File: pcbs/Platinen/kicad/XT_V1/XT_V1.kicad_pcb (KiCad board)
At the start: 4 copper layers, 100 x 77 mm, 79 parts, among them J1 Conn_01x04, J10 TBL009-500-02GY-2GY, J2 Conn_01x02, J3 Conn_01x02, J4 Conn_02x03_Odd_Even, J5 Conn_02x05_Odd_Even, J6 Conn_02x05_Odd_Even, J7 TBL009-500-02GY-2GY, J8 TBL009-500-02GY-2GY, J9 TBL009-500-02GY-2GY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

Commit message: Redesign XT V1
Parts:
- added D1: SM4007, Diode_SMD:D_MELF, F.Cu at (131.8, 86.6)
- added D2: SM4007, Diode_SMD:D_MELF, F.Cu at (137.4, 86.6)
- added Q10: BT136-500, Package_TO_SOT_THT:TO-220-3_Vertical, F.Cu at (154.7, 77.2)
- added Q9: BT136-500, Package_TO_SOT_THT:TO-220-3_Vertical, F.Cu at (144.8, 77.2)
- added R32: 330, Resistor_SMD:R_0805_2012Metric_Pad1.20x1.40mm_HandSolder, F.Cu at (156.7, 87.4)
- added R33: 56k, Resistor_SMD:R_MELF_MMB-0207, F.Cu at (131.8, 79.2)
- added R34: 56k, Resistor_SMD:R_MELF_MMB-0207, F.Cu at (137.4, 79.2)
- added R35: 68, Resistor_SMD:R_0805_2012Metric_Pad1.20x1.40mm_HandSolder, F.Cu at (121.9, 75.7)
- added R36: 68, Resistor_SMD:R_0805_2012Metric_Pad1.20x1.40mm_HandSolder, F.Cu at (142.2, 75.7)
- added R37: 68, Resistor_SMD:R_0805_2012Metric_Pad1.20x1.40mm_HandSolder, F.Cu at (152.1, 75.7)
- added U10: MOC3043M, Package_DIP:DIP-6_W8.89mm_SMDSocket_LongPads, F.Cu at (154.2, 96.3)
- added U9: MOC3043M, Package_DIP:DIP-6_W8.89mm_SMDSocket_LongPads, F.Cu at (144.3, 96.3)
- Q5, Q7: value BT136-500 -> BC846; footprint Package_TO_SOT_THT:TO-220-3_Vertical -> Package_TO_SOT_SMD:SOT-23
- R17, R18: value max 360 -> 1k
- R20, R22: value 360 -> max 360
- R23: value 360 -> 1k
- R24: value 330 -> 1k
- R26, R27: value 330 -> 360
- R28: value 68 -> 360
- R30, R31: value 68 -> 330
- U6, U8: value MOC3043M -> TLP291; footprint Package_DIP:DIP-6_W8.89mm_SMDSocket_LongPads -> Package_SO:SOIC-4_4.55x2.6mm_P1.27mm
- moved R28 38.4 mm to (151.6, 87.4), turned to 270 degrees
- moved Q5 37.7 mm to (144.3, 104.6), turned to 90 degrees
- moved R20 31.3 mm to (141.5, 104.9)
- moved Q7 30.1 mm to (154.2, 104.6), turned to 90 degrees
- moved R19 26.4 mm to (122.9, 104.9)
- moved Q4 26.4 mm to (125.7, 104.9)
- moved R15 26.4 mm to (125.7, 107.7)
- moved Q8 25.4 mm to (126.7, 77.2)
- moved R24 22.8 mm to (138.2, 101.9), turned to 0 degrees
- moved R23 22.8 mm to (131.8, 101.9), turned to 0 degrees
- moved R22 21.7 mm to (151.4, 104.9)
- moved R26 20.1 mm to (123.2, 87.4)
- moved R17 18.0 mm to (144.3, 107.4), turned to 0 degrees
- moved C16 17.6 mm to (113.8, 72.4)
- moved R30 17.2 mm to (128.3, 87.4), turned to 270 degrees
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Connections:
- J10 pad 1: Net-(J10-Pad1) -> Net-(C17-Pad2)
- J10 pad 2: Net-(J10-Pad1) -> Net-(C17-Pad2)
- J7 pad 1: Net-(J7-Pad1) -> Net-(D1-Pad2)
- J7 pad 2: Net-(J7-Pad1) -> Net-(D1-Pad2)
- J7 pad 3: Net-(C15-Pad2) -> Net-(J7-Pad3)
- J7 pad 4: Net-(C15-Pad2) -> Net-(J7-Pad3)
- J8 pad 1: Net-(J8-Pad1) -> Net-(C16-Pad2)
- J8 pad 2: Net-(J8-Pad1) -> Net-(C16-Pad2)
- J8 pad 3: Net-(C16-Pad2) -> Net-(C15-Pad2)
- J8 pad 4: Net-(C16-Pad2) -> Net-(C15-Pad2)
- J9 pad 1: Net-(J9-Pad1) -> Net-(D2-Pad2)
- J9 pad 2: Net-(J9-Pad1) -> Net-(D2-Pad2)
- J9 pad 3: Net-(C17-Pad2) -> Net-(J9-Pad3)
- J9 pad 4: Net-(C17-Pad2) -> Net-(J9-Pad3)
- Q2 pad 3: Net-(Q2-Pad3) -> ZC1
- Q3 pad 3: Net-(Q3-Pad3) -> ZC2
- Q5 pad 1: Net-(C15-Pad2) -> Net-(Q5-Pad1)
- Q5 pad 2: Net-(J7-Pad1) -> GND
- Q6 pad 2: Net-(J8-Pad1) -> Net-(D1-Pad2)
- Q7 pad 1: Net-(C17-Pad2) -> Net-(Q7-Pad1)
- Q7 pad 2: Net-(J9-Pad1) -> GND
- Q8 pad 1: Net-(C18-Pad2) -> Net-(C15-Pad2)
- Q8 pad 2: Net-(J10-Pad1) -> Net-(D1-Pad2)
- R13 pad 1: Net-(Q2-Pad1) -> +3V3
- R13 pad 2: CH2 -> ZC1
- R14 pad 1: Net-(Q3-Pad1) -> +3V3
- R14 pad 2: CH3 -> ZC2
- R15 pad 2: CH4 -> CH2
- R17 pad 1: Net-(R17-Pad1) -> Net-(Q5-Pad1)
- R17 pad 2: VCC -> CH3
- R18 pad 1: Net-(R18-Pad1) -> Net-(Q7-Pad1)
- R18 pad 2: VCC -> CH4
- R20 pad 1: Net-(J7-Pad1) -> Net-(R20-Pad1)
- R20 pad 2: Net-(R20-Pad2) -> VCC
- R21 pad 1: Net-(J8-Pad1) -> Net-(D1-Pad2)
- R22 pad 1: Net-(J9-Pad1) -> Net-(R22-Pad1)
- R22 pad 2: Net-(R22-Pad2) -> VCC
- R23 pad 1: Net-(J10-Pad1) -> Net-(R23-Pad1)
- R23 pad 2: Net-(R23-Pad2) -> Net-(Q2-Pad1)
- R24 pad 1: Net-(C15-Pad2) -> Net-(R24-Pad1)
- R24 pad 2: Net-(Q5-Pad3) -> Net-(Q3-Pad1)
- R26 pad 1: Net-(C17-Pad2) -> Net-(D1-Pad2)
- R26 pad 2: Net-(Q7-Pad3) -> Net-(R26-Pad2)
- R27 pad 1: Net-(C18-Pad2) -> Net-(D2-Pad2)
- R27 pad 2: Net-(Q8-Pad3) -> Net-(R27-Pad2)
- R28 pad 1: Net-(J7-Pad1) -> Net-(D2-Pad2)
- R28 pad 2: Net-(C15-Pad1) -> Net-(R28-Pad2)
- R29 pad 1: Net-(J8-Pad1) -> Net-(D1-Pad2)
- R30 pad 1: Net-(J9-Pad1) -> Net-(C15-Pad2)
- R30 pad 2: Net-(C17-Pad1) -> Net-(Q8-Pad3)
- R31 pad 1: Net-(J10-Pad1) -> Net-(C17-Pad2)
- R31 pad 2: Net-(C18-Pad1) -> Net-(Q9-Pad3)
- U3 pad 33: Net-(U3-Pad33) -> ZC1
- U3 pad 38: Net-(U3-Pad38) -> ZC2
- U5 pad 4: Net-(Q5-Pad3) -> Net-(Q6-Pad3)
- U5 pad 6: Net-(R20-Pad2) -> Net-(R21-Pad2)
- U6 pad 1: Net-(R17-Pad1) -> Net-(D1-Pad1)
- U6 pad 2: Net-(Q2-Pad3) -> Net-(D1-Pad2)
- U6 pad 3: Net-(U6-Pad3) -> Net-(R23-Pad1)
- U6 pad 4: Net-(Q6-Pad3) -> VCC
- U7 pad 1: Net-(R18-Pad1) -> Net-(R19-Pad1)
- U7 pad 2: Net-(Q3-Pad3) -> Net-(Q4-Pad3)
- U7 pad 4: Net-(Q7-Pad3) -> Net-(Q8-Pad3)
- U7 pad 6: Net-(R22-Pad2) -> Net-(R26-Pad2)
- U8 pad 1: Net-(R19-Pad1) -> Net-(D2-Pad1)
- U8 pad 2: Net-(Q4-Pad3) -> Net-(D2-Pad2)
- U8 pad 3: Net-(U8-Pad3) -> Net-(R24-Pad1)
- U8 pad 4: Net-(Q8-Pad3) -> VCC
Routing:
- net Net-(D1-Pad2): track 0.00 -> 74.9 mm, vias 0 -> 2
- net Net-(D2-Pad2): track 0.00 -> 72.1 mm, vias 0 -> 2
- net ZC1: track 0.00 -> 35.6 mm, vias 0 -> 2
- net ZC2: track 0.00 -> 26.8 mm, vias 0 -> 2
- net Net-(J10-Pad1): track 26.8 -> 0.00 mm
- net Net-(J8-Pad1): track 26.7 -> 0.00 mm
- net Net-(J7-Pad1): track 26.6 -> 0.00 mm
- net Net-(J9-Pad1): track 26.6 -> 0.00 mm
- net Net-(J9-Pad3): track 0.00 -> 15.5 mm
- net Net-(D1-Pad1): track 0.00 -> 13.8 mm
- net VCC: track 133.4 -> 147.1 mm, vias 5 -> 6
- net Net-(D2-Pad1): track 0.00 -> 13.4 mm
- net Net-(J7-Pad3): track 0.00 -> 13.2 mm
- net Net-(Q9-Pad3): track 0.00 -> 11.1 mm
- net Net-(Q10-Pad3): track 0.00 -> 11.1 mm
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
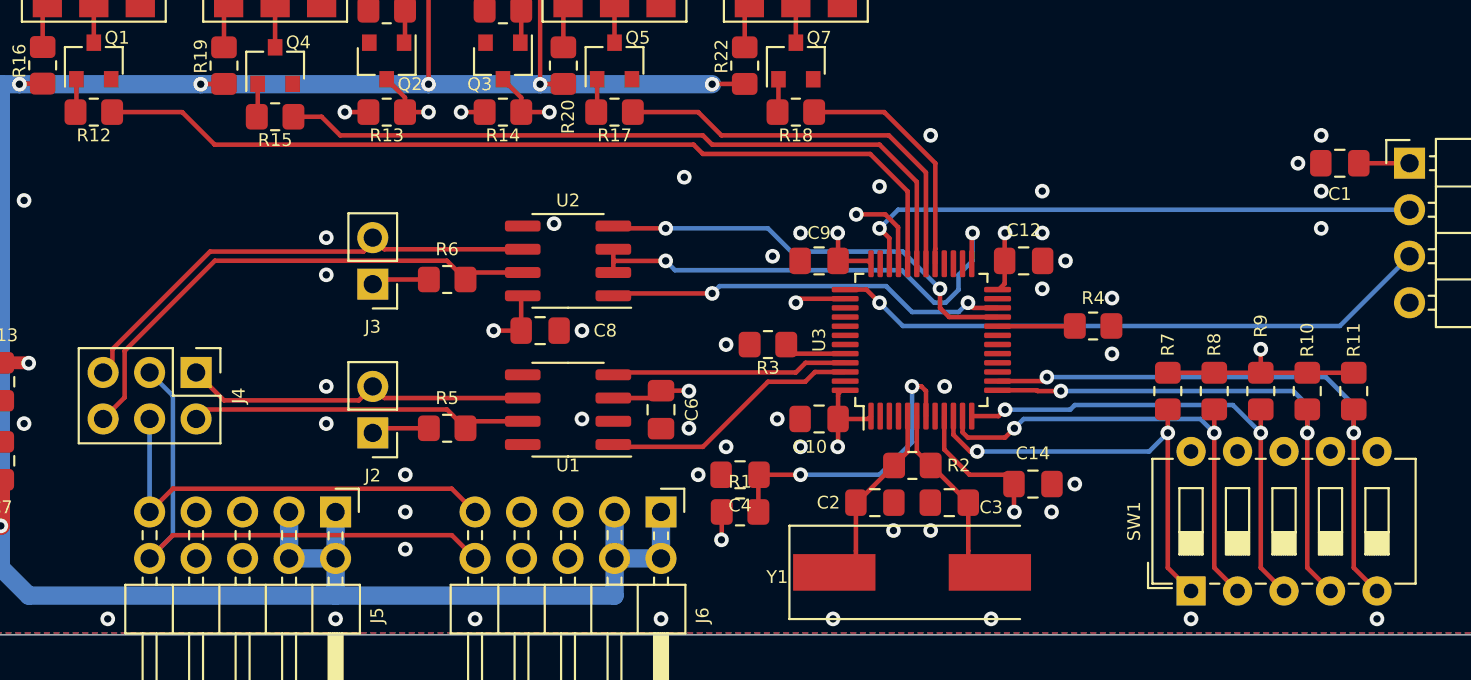
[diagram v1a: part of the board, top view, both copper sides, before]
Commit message: fix error in Schematic
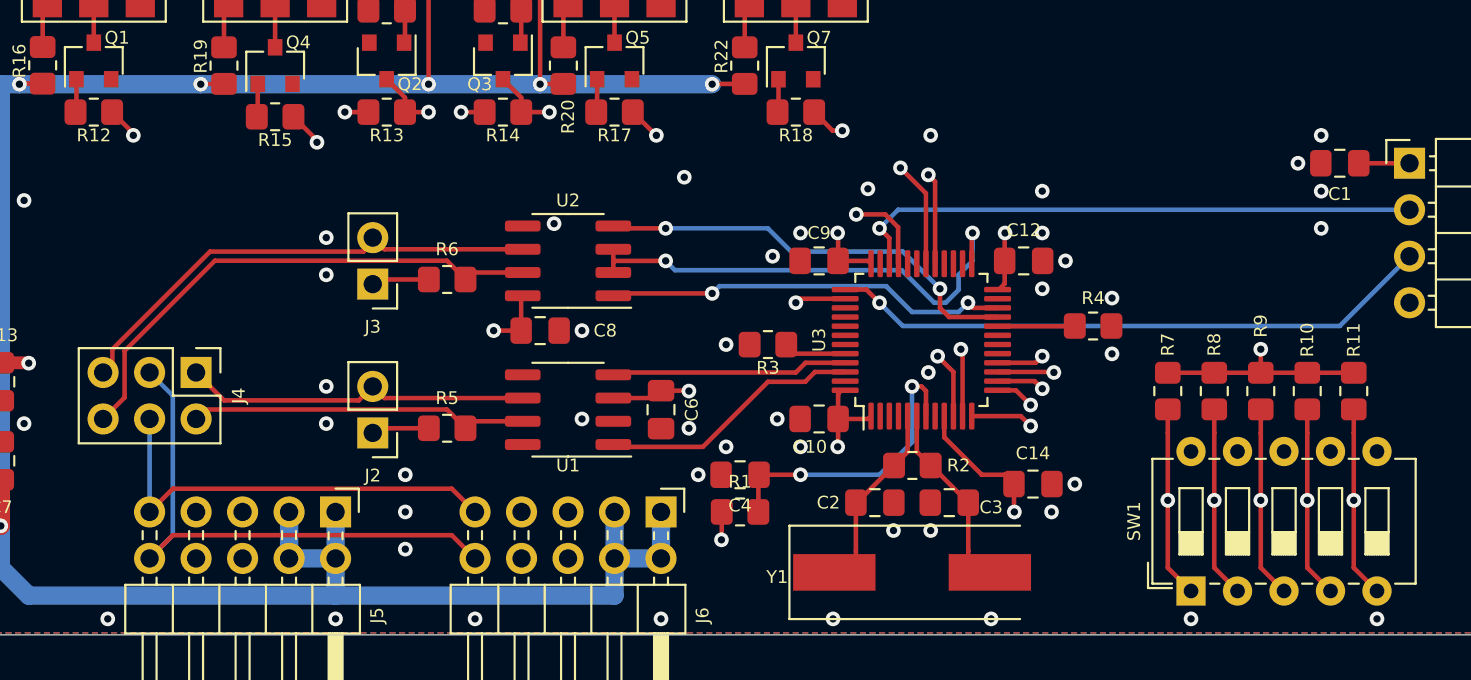
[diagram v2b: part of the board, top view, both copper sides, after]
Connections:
- U3 pad 10: Net-(R7-Pad1) -> CH3
- U3 pad 11: Net-(R8-Pad1) -> CH4
- U3 pad 12: Net-(R9-Pad1) -> Net-(R7-Pad1)
- U3 pad 13: Net-(R10-Pad1) -> Net-(R8-Pad1)
- U3 pad 14: Net-(R11-Pad1) -> Net-(R9-Pad1)
- U3 pad 15: Net-(U3-Pad15) -> Net-(R10-Pad1)
- U3 pad 16: Net-(U3-Pad16) -> Net-(R11-Pad1)
- U3 pad 29: CH4 -> CH1
- U3 pad 30: CH3 -> CH2
- U3 pad 31: CH2 -> Net-(U3-Pad31)
- U3 pad 32: CH1 -> Net-(U3-Pad32)
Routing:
- net CH4: track 13.3 -> 20.3 mm, vias 0 -> 2
- net CH3: track 22.4 -> 27.5 mm, vias 0 -> 2
- net Net-(R11-Pad1): track 31.9 -> 35.1 mm
- net Net-(R10-Pad1): track 29.0 -> 32.1 mm
- net Net-(R9-Pad1): track 26.9 -> 29.4 mm
- net CH1: track 49.2 -> 51.4 mm, vias 0 -> 2
- net Net-(R8-Pad1): track 25.7 -> 26.6 mm
- net Net-(R7-Pad1): track 23.7 -> 22.8 mm
- net CH2: track 40.0 -> 40.2 mm, vias 0 -> 2

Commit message: started revs
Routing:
- net DIR: track 26.5 -> 28.6 mm
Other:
- board text added: "Marco Müller revved by Blind_Via"
- board text removed: "Marco Müller not revved by theBrutzler yet"

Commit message: complete reviews from dave
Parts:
- added REF**: ESD-Logo_6.6x6mm_SilkScreen, Symbol:ESD-Logo_6.6x6mm_SilkScreen, F.Cu at (182.1, 89.7)
- moved REF** 4.83 mm to (172.7, 89.7)

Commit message: greate gerbers, plot schematics
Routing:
- net Net-(J9-Pad3): track 15.5 -> 16.5 mm
- net Net-(C17-Pad2): track 28.1 -> 28.9 mm
